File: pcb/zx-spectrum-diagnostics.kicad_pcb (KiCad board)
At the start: 2 copper layers, 99.9 x 98.2 mm, 74 parts, among them J101 Conn_01x04, J201 Conn_01x20_Female, J202 Conn_01x20_Female, J203 Conn_01x20_Female, J205 Conn_01x20_Female, Q101 PMBT2222A, SW101 SW_SPST, SW102 SW_SPST, U101 Pico, U102 Pico

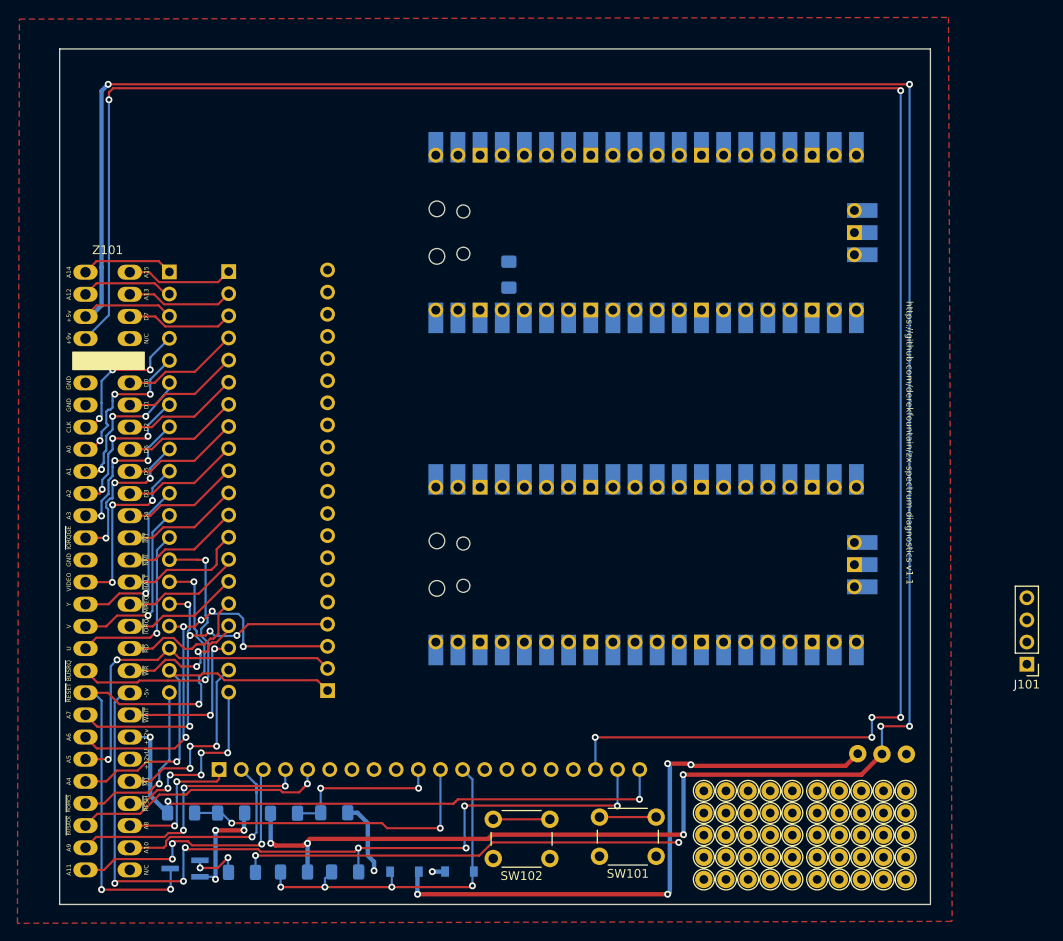
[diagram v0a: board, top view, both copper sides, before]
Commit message: just realised i've left J205 on the PCB! need to remove it and tidy up
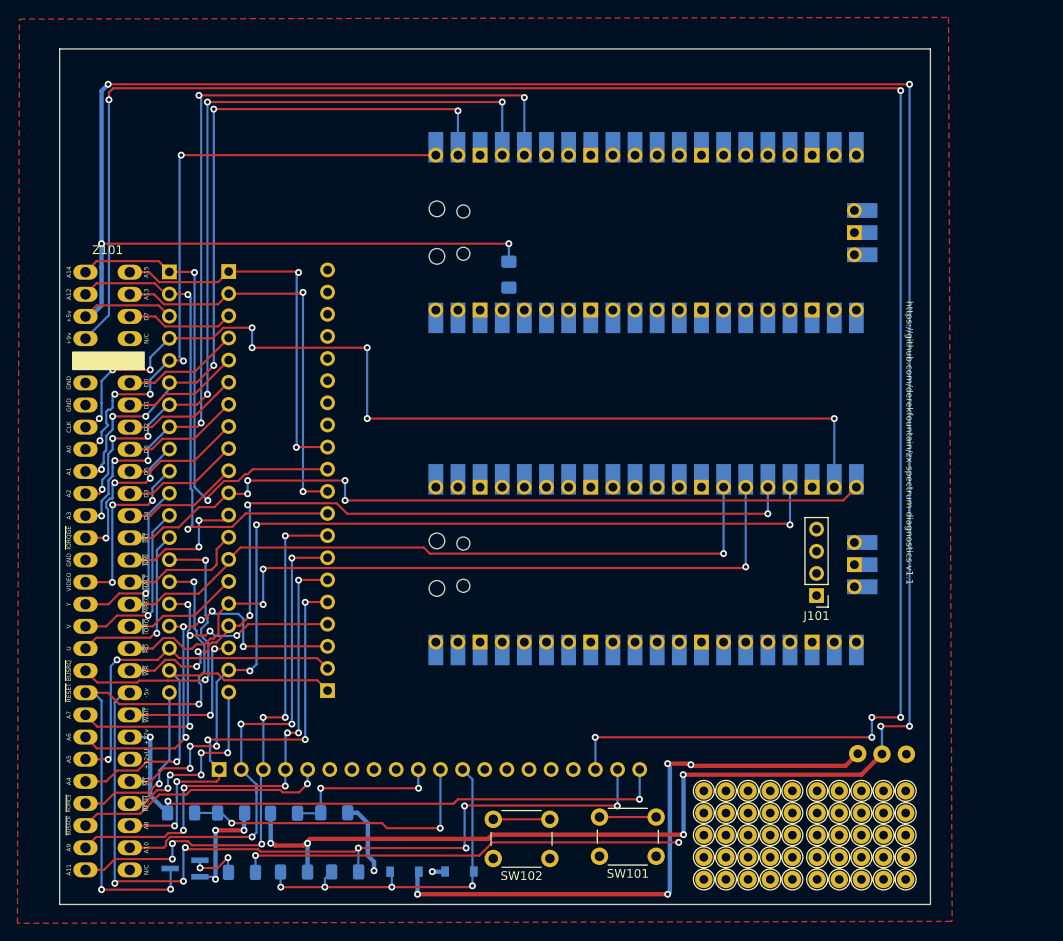
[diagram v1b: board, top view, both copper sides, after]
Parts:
- moved J101 25.4 mm to (161.5, 118.6)
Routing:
- net ZXCLK: track 17.1 -> 112.2 mm, vias 3 -> 8
- net ZXA3: track 17.6 -> 103.1 mm, vias 3 -> 6
- net ZXM1: track 22.4 -> 107.6 mm, vias 3 -> 6
- net ZXWR: track 15.8 -> 94.9 mm, vias 2 -> 5
- net ZXA2: track 17.4 -> 95.7 mm, vias 3 -> 6
- net ZXINT: track 13.5 -> 90.0 mm, vias 0 -> 4
- net ZXRD: track 15.8 -> 88.5 mm, vias 0 -> 3
- net ZXA1: track 17.2 -> 85.7 mm, vias 3 -> 6
- net ZXMREQ: track 13.8 -> 79.1 mm, vias 0 -> 1
- net ZXA0: track 17.3 -> 72.0 mm, vias 3 -> 5
- net +5V: track 295.3 -> 344.1 mm, vias 8 -> 10
- net ZXA12: track 10.2 -> 56.5 mm, vias 0 -> 2
- net ZXA14: track 10.7 -> 55.8 mm, vias 0 -> 2
- net ZXA13: track 12.3 -> 46.6 mm, vias 0 -> 2
- net ZXA10: track 24.5 -> 58.8 mm, vias 1 -> 4
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
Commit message: connections all in place, many tidyups required
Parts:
- removed J205: Conn_01x20_Female, Connector_PinSocket_2.54mm:PinSocket_1x20_P2.54mm_Vertical
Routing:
- net P2_GPIO18: track 0.00 -> 120.1 mm, vias 0 -> 6
- net P2_GPIO16: track 0.00 -> 119.8 mm, vias 0 -> 5
- net P2_GPIO17: track 0.00 -> 118.7 mm, vias 0 -> 6
- net PICO_SIGNAL: track 0.00 -> 102.9 mm, vias 0 -> 6
- net ZXA7: track 45.7 -> 144.2 mm, vias 5 -> 8
- net ZXA8: track 49.9 -> 146.1 mm, vias 5 -> 8
- net ZXA10: track 58.8 -> 151.2 mm, vias 4 -> 7
- net ZXA11: track 65.8 -> 157.5 mm, vias 6 -> 9
- net ZXA6: track 48.2 -> 137.8 mm, vias 5 -> 8
- net ZXA9: track 57.0 -> 145.9 mm, vias 6 -> 9
- net ZXA4: track 41.8 -> 126.7 mm, vias 1 -> 4
- net ZXA5: track 41.3 -> 126.1 mm, vias 2 -> 5
- net P2_BLIPPER: track 0.00 -> 82.1 mm, vias 0 -> 2
- net 3V3_PICO1: track 68.8 -> 142.3 mm, vias 4 -> 9
- net ZXD7: track 12.3 -> 78.7 mm, vias 0 -> 3
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
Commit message: v1.1 ready to go? last checks
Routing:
- net ZXA4: track 126.7 -> 124.2 mm
- net ZXRD: track 88.5 -> 86.2 mm
- net ZXA1: track 85.7 -> 83.6 mm, vias 6 -> 5
- net P2_GPIO18: track 120.1 -> 118.0 mm
- net ZXD4: track 52.0 -> 50.0 mm
- net ZXVIDEO: track 21.0 -> 19.1 mm, vias 3 -> 2
- net P2_GPIO17: track 118.7 -> 116.9 mm
- net ZXA2: track 95.7 -> 94.1 mm, vias 6 -> 5
- net ZXMIN5V: track 96.9 -> 95.2 mm
- net P2_GPIO16: track 119.8 -> 118.2 mm
- net ZXA7: track 144.2 -> 142.6 mm, vias 8 -> 5
- net ZXA3: track 103.1 -> 101.6 mm, vias 6 -> 5
- net +5V: track 344.4 -> 345.8 mm
- net ZXA10: track 151.2 -> 149.8 mm
- net ZXIORQGE: track 18.0 -> 16.6 mm, vias 3 -> 2
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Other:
- board text added: "+12V"
- board text added: "P1 BLIP"
- board text added: "P2 BLIP"
- board text added: "P2_G16"
- board text added: "P2_G17"
- board text added: "P2_G18"
- board text added: "P2_G26"
- board text added: "P2_G27"
- board text added: "P2_G28"
- board text added: "PICO SIG"
- board text removed: "12V"
- board text removed: "12VAC"
- board text removed: "Y"

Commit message: v1.1 off for fabrication
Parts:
- added ?: , , F.Cu at (109.2, 128.8)
- added ?: , , F.Cu at (112.8, 128.8)
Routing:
- net P1_BLIPPER: track 57.7 -> 73.2 mm
- net P2_BLIPPER: track 82.1 -> 96.0 mm, vias 2 -> 3
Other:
- board text added: "OLED CLK"
- board text added: "OLED SDA"
- board text added: "P1 BLIPPER"
- board text added: "P2 BLIPPER"
- board text added: "Y"
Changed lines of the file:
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@@
   (paper "A4")
   (title_block
+    (title "ZX Spectrum Diagnostics")
     (date "2023-11-30")
+    (rev "1.1")
   )
   (layers
@@
       (usegerberattributes true)
       (usegerberadvancedattributes true)
-      (creategerberjobfile true)
+      (creategerberjobfile false)
       (svguseinch false)
       (svgprecision 6)
@@
       (drillshape 0)
       (scaleselection 1)
-      (outputdirectory "./fab1.0")
+      (outputdirectory "./fab1.1")
     )
   )
@@
     (pad "1" thru_hole circle (at 0 0) (size 2 2) (drill 1) (layers F&B.Cu *.Mask))
   )
+  (footprint "" (layer "F.Cu")
+    (at 109.22 128.778)
+    (fp_text reference "" (at 0 0) (layer "F.SilkS")
+      (effects (font (size 1.27 1.27) (thickness 0.15)))
+    )
+    (fp_text value "" (at 0 0) (layer "F.SilkS")
+      (effects (font (size 1.27 1.27) (thickness 0.15)))
+    )
+    (pad "1" thru_hole circle (at 0 0) (size 2 2) (drill 1) (layers *.Cu *.Mask)
+      (net 19 "P1_BLIPPER"))
+  )
   (footprint "TestPoint:TestPoint_THTPad_D2.0mm_Drill1.0mm" (layer "F.Cu")
     (at 158.77 148.64)
@@
     (pad "1" thru_hole circle (at 0 0) (size 2 2) (drill 1) (layers F&B.Cu *.Mask))
   )
+  (footprint "" (layer "F.Cu")
+    (at 112.776 128.778)
+    (fp_text reference "" (at 0 0) (layer "F.SilkS")
+      (effects (font (size 1.27 1.27) (thickness 0.15)))
+    )
+    (fp_text value "" (at 0 0) (layer "F.SilkS")
+      (effects (font (size 1.27 1.27) (thickness 0.15)))
+    )
+    (pad "1" thru_hole circle (at 0 0) (size 2 2) (drill 1) (layers *.Cu *.Mask)
+      (net 20 "P2_BLIPPER"))
+  )
   (footprint "TestPoint:TestPoint_THTPad_D2.0mm_Drill1.0mm" (layer "F.Cu")
     (at 169.23 148.64)
@@
     (effects (font (size 0.8 0.8) (thickness 0.125)) (justify right mirror))
   )
-  (gr_text "VIDEO" (at 89.128 106.79 330) (layer "B.SilkS")
+  (gr_text "Y" (at 89.128 106.79 330) (layer "B.SilkS")
     (effects (font (size 0.8 0.8) (thickness 0.125)) (justify right mirror))
   )
@@
     (effects (font (size 0.8 0.8) (thickness 0.125)) (justify right mirror))
   )
+  (gr_text "GND" (at 164.338 110.744) (layer "F.SilkS")
+    (effects (font (size 0.8 0.8) (thickness 0.15)))
+  )
   (gr_text "https://github.com/derekfountain/zx-spectrum-diagnostics v1.1" (at 172.212 101.092 270) (layer "F.SilkS")
     (effects (font (size 0.75 0.75) (thickness 0.15)))
   )
+  (gr_text "OLED SDA" (at 157.226 118.872) (layer "F.SilkS")
+    (effects (font (size 0.8 0.8) (thickness 0.15)))
+  )
+  (gr_text "P2 BLIPPER" (at 112.776 122.936 -90) (layer "F.SilkS")
+    (effects (font (size 1 1) (thickness 0.15)))
+  )
+  (gr_text "OLED CLK" (at 157.226 116.078) (layer "F.SilkS")
+    (effects (font (size 0.8 0.8) (thickness 0.15)))
+  )
+  (gr_text "P1 BLIPPER" (at 108.966 122.936 -90) (layer "F.SilkS")
+    (effects (font (size 1 1) (thickness 0.15)))
+  )
   (gr_text "Some 3216 footprints with tracks coming from them \nmight be more useful than all these test points?\nIf I want to mount SMD diodes or something?" (at 160.208 160.752) (layer "Cmts.User")
     (effects (font (size 1 1) (thickness 0.15)))
@@
   (segment (start 105.69 138.565) (end 105.69 136.424) (width 0.25) (layer "B.Cu") (net 18))
   (segment (start 105.69 136.424) (end 105.664 136.398) (width 0.25) (layer "B.Cu") (net 18))
+  (segment (start 114.808 129.54) (end 113.538 130.81) (width 0.25) (layer "F.Cu") (net 19))
+  (segment (start 113.538 130.81) (end 111.252 130.81) (width 0.25) (layer "F.Cu") (net 19))
+  (segment (start 111.252 130.81) (end 109.22 128.778) (width 0.25) (layer "F.Cu") (net 19))
   (segment (start 123.444 129.54) (end 147.066 129.54) (width 0.25) (layer "F.Cu") (net 19))
+  (segment (start 123.444 129.54) (end 114.808 129.54) (width 0.25) (layer "F.Cu") (net 19))
   (segment (start 147.066 112.522) (end 145.542 112.522) (width 0.25) (layer "F.Cu") (net 19))
   (via (at 123.444 129.54) (size 0.8) (drill 0.4) (layers "F.Cu" "B.Cu") (net 19))
@@
   (segment (start 155.702 93.98) (end 155.956 93.726) (width 0.25) (layer "F.Cu") (net 20))
   (segment (start 126.746 93.98) (end 155.702 93.98) (width 0.25) (layer "F.Cu") (net 20))
+  (segment (start 126.746 128.778) (end 112.776 128.778) (width 0.25) (layer "F.Cu") (net 20))
   (via (at 126.746 93.98) (size 0.8) (drill 0.4) (layers "F.Cu" "B.Cu") (net 20))
   (via (at 155.956 93.726) (size 0.8) (drill 0.4) (layers "F.Cu" "B.Cu") (net 20))
-  (segment (start 126.746 137.829) (end 126.746 93.98) (width 0.25) (layer "B.Cu") (net 20))
+  (via (at 126.746 128.778) (size 0.8) (drill 0.4) (layers "F.Cu" "B.Cu") (net 20))
+  (segment (start 126.746 128.778) (end 126.746 93.98) (width 0.25) (layer "B.Cu") (net 20))
+  (segment (start 126.746 137.829) (end 126.746 128.778) (width 0.25) (layer "B.Cu") (net 20))
   (segment (start 126.01 138.565) (end 126.746 137.829) (width 0.25) (layer "B.Cu") (net 20))
   (segment (start 155.956 93.726) (end 155.956 85.852) (width 0.25) (layer "B.Cu") (net 20))
